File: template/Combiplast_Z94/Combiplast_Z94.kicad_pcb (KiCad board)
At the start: 2 copper layers, 59 x 37 mm, 4 parts

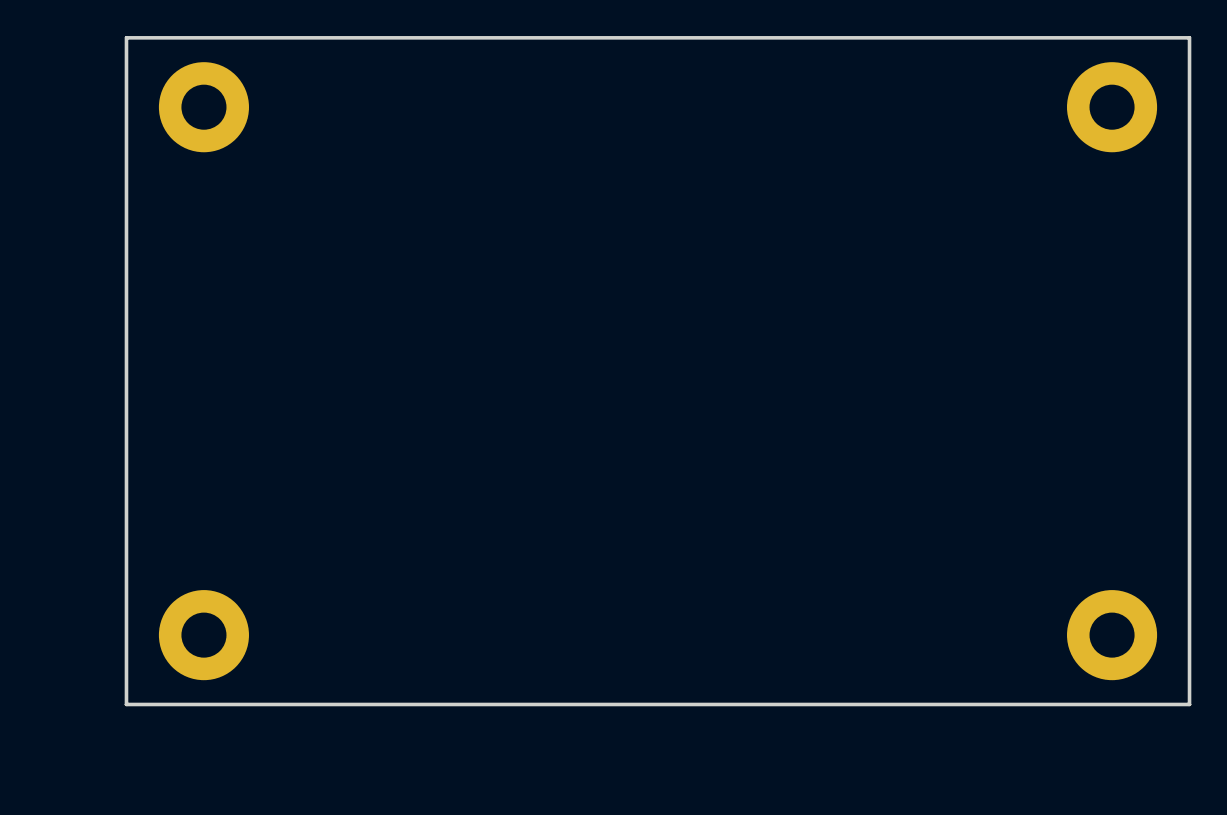
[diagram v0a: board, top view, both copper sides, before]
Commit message: Updated templates
Added mounting holes on schematics, dimensions and re-adjusted board
sizes
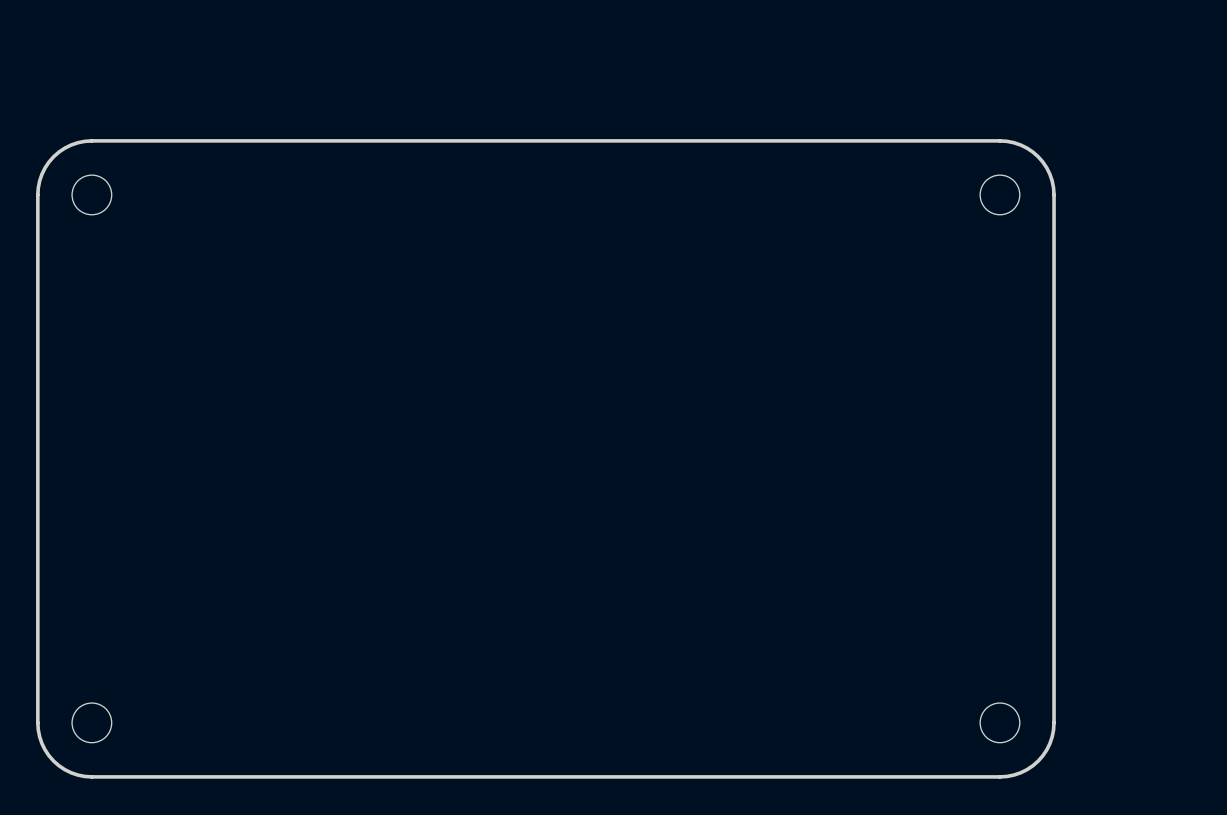
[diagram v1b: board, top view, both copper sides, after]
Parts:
- removed REF** (x4): MountingHole_2.5mm_Pad, MountingHole:MountingHole_2.5mm_Pad
- added H1: MountingHole, MountingHole:MountingHole_2.2mm_M2, F.Cu at (120.0, 90.0)
- added H2: MountingHole, MountingHole:MountingHole_2.2mm_M2, F.Cu at (170.4, 90.0)
- added H3: MountingHole, MountingHole:MountingHole_2.2mm_M2, F.Cu at (120.0, 119.3)
- added H4: MountingHole, MountingHole:MountingHole_2.2mm_M2, F.Cu at (170.4, 119.3)
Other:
- board size 59 x 37 mm -> 56.4 x 35.3 mm
